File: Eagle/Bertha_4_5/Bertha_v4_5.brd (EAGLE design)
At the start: 100 x 83.6 mm, 137 parts, among them CON1 JACK_DC_BARREL, CON2 JACK_DC_BARREL, IC1 MCP1703DB, IC4 DRV8811, J1 RJ12RIGHTANGLE-I2C, J2 RJ12RIGHTANGLE-I2C, Q5 BSP75, Q6 BSP75, U1 HX711, X1 1503_09, X2 8MHz, X3 FH12-08S-1SH, X4 MINI-USB

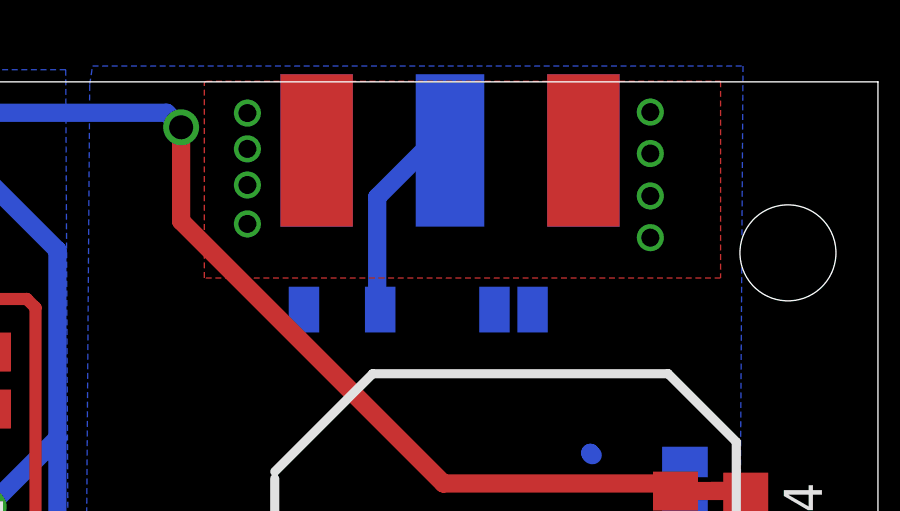
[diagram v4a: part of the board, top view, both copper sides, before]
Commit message: changed the SMA edge connector forrpting fot LoRa antenna. Foortptint to be checked, Gerbers to be Regenerated !
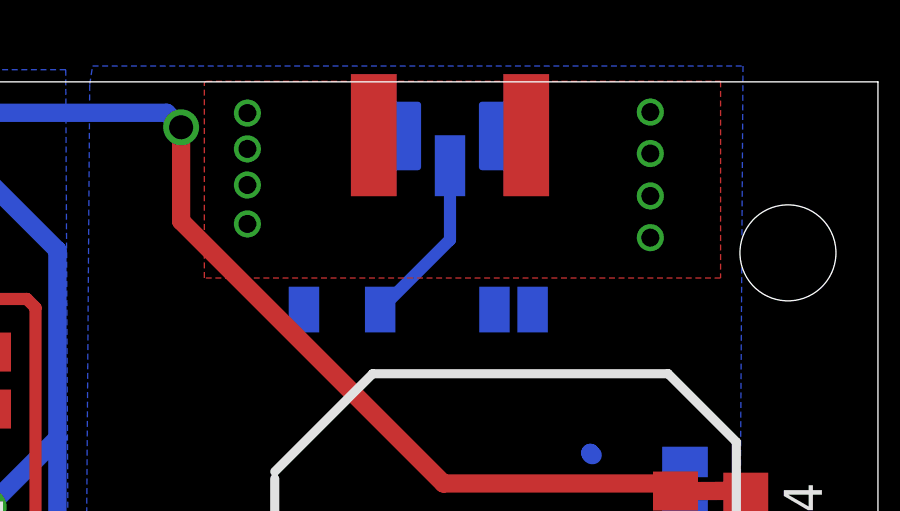
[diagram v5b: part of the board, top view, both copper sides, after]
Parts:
- 868MHZ: device sma_end_launch:SMA_EDGELAUNCH -> sma_end_launch:SMA_EDGELAUNCH_UFL
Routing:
- net ANT868: track 6.89 -> 5.90 mm
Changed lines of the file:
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@@
 </element>
 <element name="3V3" library="Headerlibrary" package="1X01" value="" x="24.84389375" y="29.06728125"/>
-<element name="868MHZ" library="sma_end_launch" package="SMA_EDGELAUNCH" value="" x="80.734909375" y="81.954096875" rot="MR270"/>
+<element name="868MHZ" library="sma_end_launch" package="SMA_EDGELAUNCH_UFL" value="" x="80.734909375" y="81.954096875" rot="MR270"/>
 <element name="D1" library="lpatiny" package="LED-1206" value="1N581D1206" x="8.85254375" y="10.442784375" smashed="yes" rot="MR0">
 <attribute name="NAME" x="9.74154375" y="11.839784375" size="0.4064" layer="26" rot="MR0"/>
@@
 <signal name="ANT868">
 <contactref element="868MHZ" pad="P"/>
-<wire x1="79.926053125" y1="79.4735625" x2="78.3081375" y2="77.855646875" width="0.6096" layer="16"/>
-<wire x1="79.926053125" y1="79.4735625" x2="80.734909375" y2="79.414096875" width="0.6096" layer="16"/>
 <contactref element="U$3" pad="P$23"/>
-<wire x1="78.3081375" y1="74.209425" x2="78.40780625" y2="74.10975625" width="0.6096" layer="16"/>
-<wire x1="78.3081375" y1="77.855646875" x2="78.3081375" y2="74.209425" width="0.6096" layer="16"/>
+<wire x1="78.40780625" y1="74.10975625" x2="78.3081375" y2="74.209425" width="0.6096" layer="16"/>
+<wire x1="80.734909375" y1="78.906096875" x2="80.734909375" y2="76.436859375" width="0.4064" layer="16"/>
+<wire x1="80.734909375" y1="76.436859375" x2="78.40780625" y2="74.10975625" width="0.4064" layer="16"/>
 </signal>
 <signal name="N$8">
@@
 <wire x1="85.896671875" y1="50.372284375" x2="85.896671875" y2="51.700603125" width="0.4064" layer="16"/>
 <wire x1="83.586675" y1="50.348665625" x2="83.586675" y2="51.750825" width="0.4064" layer="16"/>
+<contactref element="868MHZ" pad="GND@4"/>
+<contactref element="868MHZ" pad="GND@3"/>
+<contactref element="868MHZ" pad="GND@2"/>
 <contactref element="868MHZ" pad="GND@1"/>
-<contactref element="868MHZ" pad="GND@2"/>
-<contactref element="868MHZ" pad="GND@3"/>
-<contactref element="868MHZ" pad="GND@4"/>
 <via x="73.981253125" y="80.659584375" extent="1-16" drill="0.6"/>
 <via x="73.981253125" y="79.4663125" extent="1-16" drill="0.6"/>
